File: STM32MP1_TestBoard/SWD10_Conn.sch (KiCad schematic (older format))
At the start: 1 part

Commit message: updated bom, readme
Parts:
- J1: renamed from J?; footprint (none) -> Connector_PinHeader_1.27mm:PinHeader_2x05_P1.27mm_Vertical_SMD; Mfr (none) -> Amphenol ICC; PartNo (none) -> 20021121-00010C4LF
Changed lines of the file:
@@
 $Descr A4 11693 8268
 encoding utf-8
-Sheet 5 9
+Sheet 6 9
 Title ""
 Date ""
@@
 P 5125 3750
 AR Path="/5FBD70AB/60D84783" Ref="J?"  Part="1"
-AR Path="/5FBD70AB/60D82D6A/60D84783" Ref="J?"  Part="1"
-AR Path="/60DBD4A2/60D84783" Ref="J?"  Part="1"
-F 0 "J?" H 5175 4167 50  0000 C CNN
+AR Path="/5FBD70AB/60D82D6A/60D84783" Ref="J1"  Part="1"
+AR Path="/60DBD4A2/60D84783" Ref="J2"  Part="1"
+F 0 "J2" H 5175 4167 50  0000 C CNN
 F 1 "Conn_02x05_Odd_Even" H 5175 4076 50  0000 C CNN
-F 2 "" H 5125 3750 50  0001 C CNN
-F 3 "~" H 5125 3750 50  0001 C CNN
+F 2 "Connector_PinHeader_1.27mm:PinHeader_2x05_P1.27mm_Vertical_SMD" H 5125 3750 50  0001 C CNN
+F 3 "https://docs.rs-online.com/75e3/0900766b8142184e.pdf" H 5125 3750 50  0001 C CNN
+F 4 "Amphenol ICC" H 5125 3750 50  0001 C CNN "Mfr"
+F 5 "20021121-00010C4LF" H 5125 3750 50  0001 C CNN "PartNo"
 	1    5125 3750
 	1    0    0    -1
@@
 P 4475 3225
 AR Path="/5FBD70AB/60D8478B" Ref="#PWR?"  Part="1"
-AR Path="/5FBD70AB/60D82D6A/60D8478B" Ref="#PWR?"  Part="1"
-AR Path="/60DBD4A2/60D8478B" Ref="#PWR?"  Part="1"
-F 0 "#PWR?" H 4475 3075 50  0001 C CNN
+AR Path="/5FBD70AB/60D82D6A/60D8478B" Ref="#PWR0116"  Part="1"
+AR Path="/60DBD4A2/60D8478B" Ref="#PWR0118"  Part="1"
+F 0 "#PWR0118" H 4475 3075 50  0001 C CNN
 F 1 "+3V3" H 4490 3398 50  0000 C CNN
 F 2 "" H 4475 3225 50  0001 C CNN
@@
 P 4475 4150
 AR Path="/5FBD70AB/60D84794" Ref="#PWR?"  Part="1"
-AR Path="/5FBD70AB/60D82D6A/60D84794" Ref="#PWR?"  Part="1"
-AR Path="/60DBD4A2/60D84794" Ref="#PWR?"  Part="1"
-F 0 "#PWR?" H 4475 3900 50  0001 C CNN
+AR Path="/5FBD70AB/60D82D6A/60D84794" Ref="#PWR0117"  Part="1"
+AR Path="/60DBD4A2/60D84794" Ref="#PWR0119"  Part="1"
+F 0 "#PWR0119" H 4475 3900 50  0001 C CNN
 F 1 "GNDS" H 4480 3977 50  0000 C CNN
 F 2 "" H 4475 4150 50  0001 C CNN

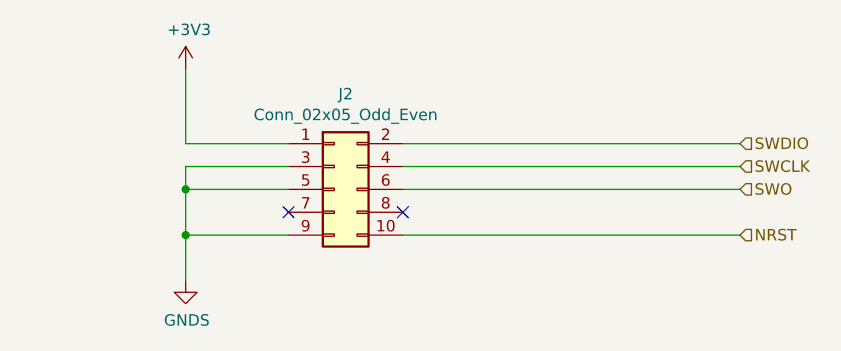
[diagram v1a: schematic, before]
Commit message: updated schematic design
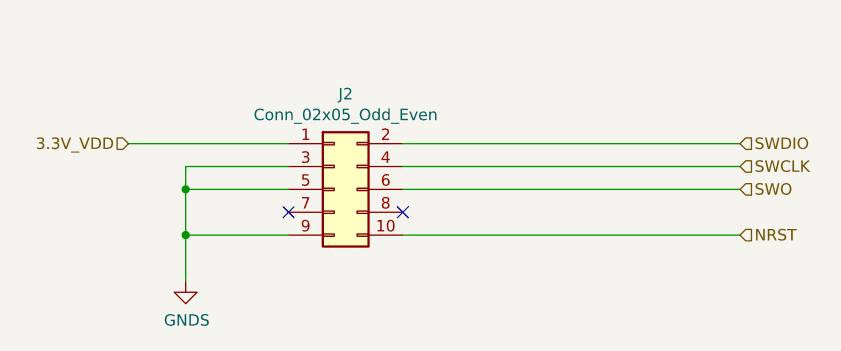
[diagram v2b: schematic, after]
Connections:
- net +3V3 renamed 3.3V_VDD
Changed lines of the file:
@@
 $Descr A4 11693 8268
 encoding utf-8
-Sheet 6 9
+Sheet 6 10
 Title ""
 Date ""
@@
 AR Path="/5FBD70AB/60D82D6A/60D84783" Ref="J1"  Part="1"
 AR Path="/60DBD4A2/60D84783" Ref="J2"  Part="1"
+AR Path="/606F7DFA/606FAC2E/60D84783" Ref="J2"  Part="1"
 F 0 "J2" H 5175 4167 50  0000 C CNN
 F 1 "Conn_02x05_Odd_Even" H 5175 4076 50  0000 C CNN
@@
 F 5 "20021121-00010C4LF" H 5125 3750 50  0001 C CNN "PartNo"
 	1    5125 3750
-	1    0    0    -1
-$EndComp
-Wire Wire Line
-	4925 3550 4475 3550
-Wire Wire Line
-	4475 3550 4475 3225
-$Comp
-L power:+3V3 #PWR?
-U 1 1 60D8478B
-P 4475 3225
-AR Path="/5FBD70AB/60D8478B" Ref="#PWR?"  Part="1"
-AR Path="/5FBD70AB/60D82D6A/60D8478B" Ref="#PWR0116"  Part="1"
-AR Path="/60DBD4A2/60D8478B" Ref="#PWR0118"  Part="1"
-F 0 "#PWR0118" H 4475 3075 50  0001 C CNN
-F 1 "+3V3" H 4490 3398 50  0000 C CNN
-F 2 "" H 4475 3225 50  0001 C CNN
-F 3 "" H 4475 3225 50  0001 C CNN
-	1    4475 3225
 	1    0    0    -1
 $EndComp
@@
 AR Path="/5FBD70AB/60D82D6A/60D84794" Ref="#PWR0117"  Part="1"
 AR Path="/60DBD4A2/60D84794" Ref="#PWR0119"  Part="1"
-F 0 "#PWR0119" H 4475 3900 50  0001 C CNN
+AR Path="/606F7DFA/606FAC2E/60D84794" Ref="#PWR019"  Part="1"
+F 0 "#PWR019" H 4475 3900 50  0001 C CNN
 F 1 "GNDS" H 4480 3977 50  0000 C CNN
 F 2 "" H 4475 4150 50  0001 C CNN
@@
 NoConn ~ 5425 3850
 Wire Wire Line
-	6900 3950 5425 3950
-Wire Wire Line
 	5425 3550 6900 3550
 Wire Wire Line
@@
 Text HLabel 6900 3950 2    50   Input ~ 0
 NRST
+Wire Wire Line
+	5425 3950 6900 3950
+Text HLabel 4225 3550 0    50   Input ~ 0
+3.3V_VDD
+Wire Wire Line
+	4225 3550 4925 3550
 $EndSCHEMATC

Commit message: added traces for sdio, dsi and swd connectors
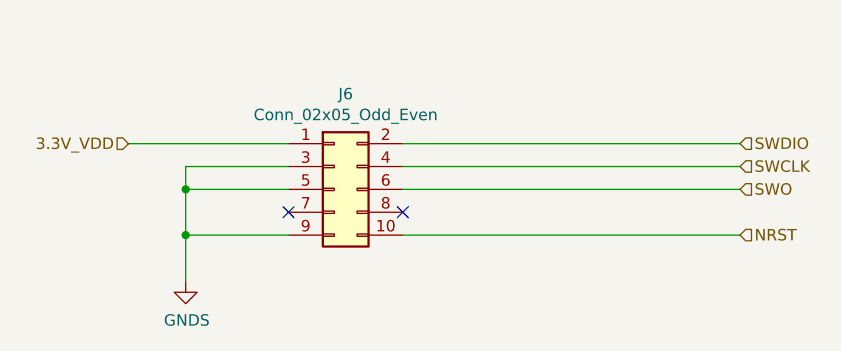
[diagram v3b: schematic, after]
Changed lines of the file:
@@
 $Descr A4 11693 8268
 encoding utf-8
-Sheet 6 10
+Sheet 5 10
 Title ""
 Date ""
@@
 AR Path="/5FBD70AB/60D82D6A/60D84783" Ref="J1"  Part="1"
 AR Path="/60DBD4A2/60D84783" Ref="J2"  Part="1"
-AR Path="/606F7DFA/606FAC2E/60D84783" Ref="J2"  Part="1"
-F 0 "J2" H 5175 4167 50  0000 C CNN
+AR Path="/606F7DFA/606FAC2E/60D84783" Ref="J6"  Part="1"
+F 0 "J6" H 5175 4167 50  0000 C CNN
 F 1 "Conn_02x05_Odd_Even" H 5175 4076 50  0000 C CNN
 F 2 "Connector_PinHeader_1.27mm:PinHeader_2x05_P1.27mm_Vertical_SMD" H 5125 3750 50  0001 C CNN
